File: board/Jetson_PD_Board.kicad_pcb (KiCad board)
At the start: 2 copper layers, 41.5 x 34.5 mm, 47 parts, among them J1 USB4081-03-A, J2 768250002, Q1 NTTFS5C673NLTAG, Q2 NTTFS5C673NLTAG, Q3 NTTFS5C673NLTAG, U1 APK43070DKZ-13-FA01, U2 USBLC6-2SC6

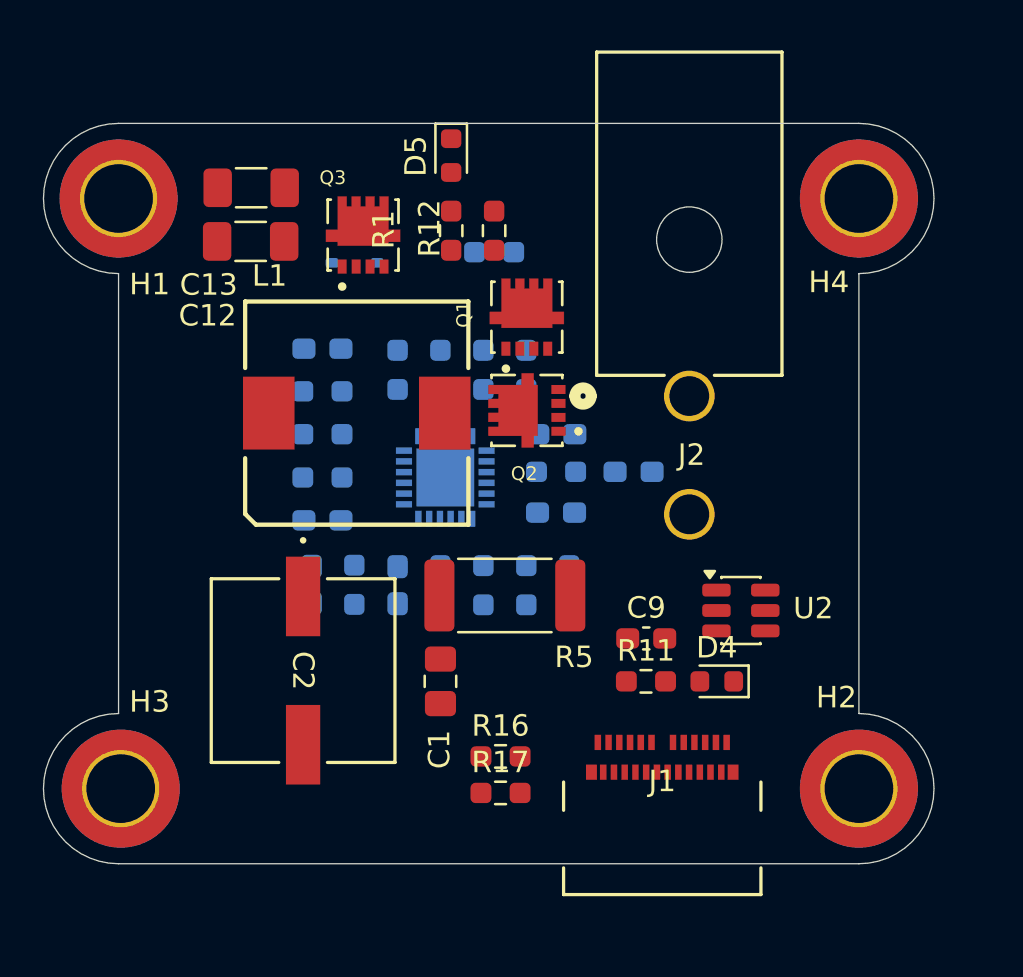
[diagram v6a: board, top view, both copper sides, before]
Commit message: Arranged power components
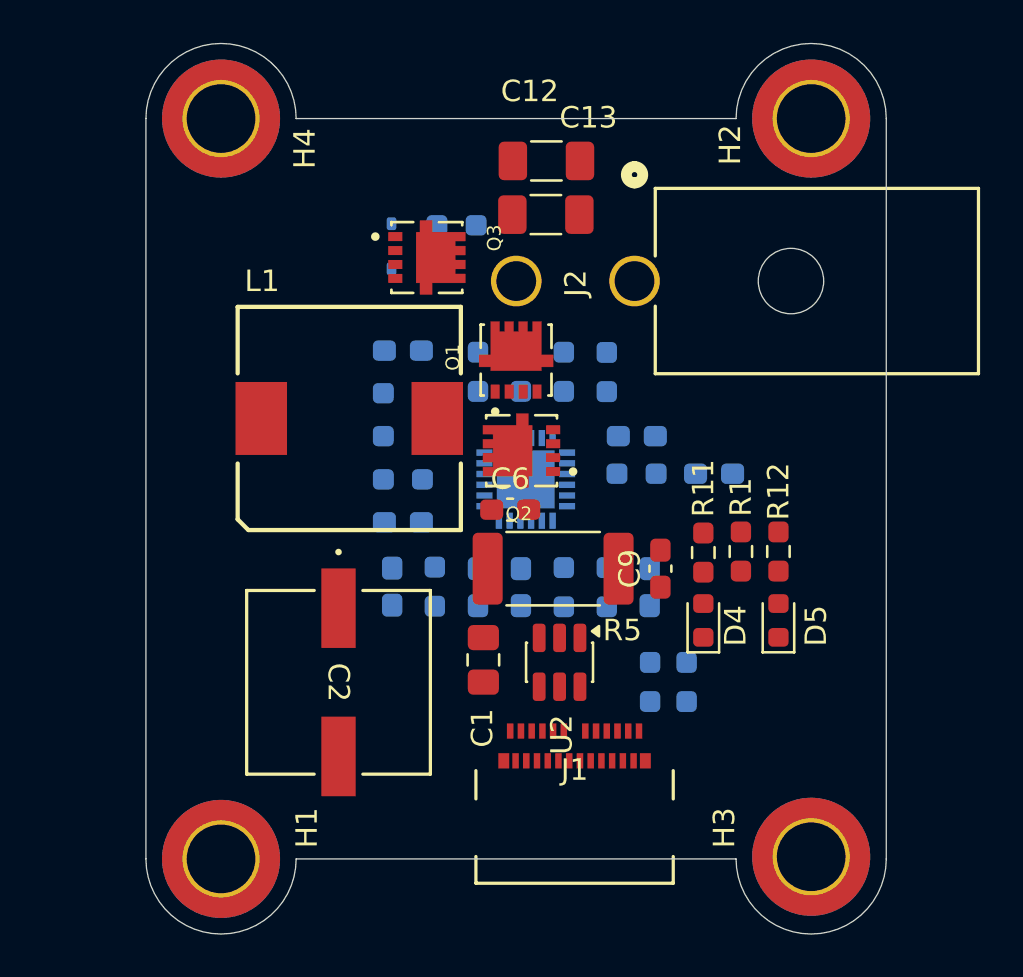
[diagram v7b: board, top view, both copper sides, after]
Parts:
- C6: moved to F.Cu
- R16, R17: moved to B.Cu
- moved H3 32.3 mm to (137.3, 114.7), turned to 90 degrees
- moved H2 31.3 mm to (137.3, 80.3), turned to -90 degrees
- moved H1 31.1 mm to (109.8, 114.8), turned to -90 degrees
- moved H4 30.0 mm to (109.8, 80.3), turned to 90 degrees
- moved D5 26.5 mm to (135.8, 103.7), turned to 90 degrees
- moved R1 20.1 mm to (134.0, 100.5)
- moved R12 20.0 mm to (135.8, 100.5)
- moved C12 14.3 mm to (124.9, 82.2), turned to 0 degrees
- moved C13 13.8 mm to (124.9, 84.8), turned to 0 degrees
- moved R17 10.1 mm to (131.5, 106.5), turned to -90 degrees
- moved U2 8.79 mm to (125.5, 105.6), turned to -90 degrees
- moved R16 7.79 mm to (129.8, 106.5), turned to -90 degrees
- moved R11 6.57 mm to (132.2, 100.5), turned to -90 degrees
- moved J2 5.94 mm to (129.0, 87.8), turned to 90 degrees
- moved J1 4.12 mm to (126.2, 112.2)
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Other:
- board size 41.5 x 34.5 mm -> 34.5 x 41.5 mm

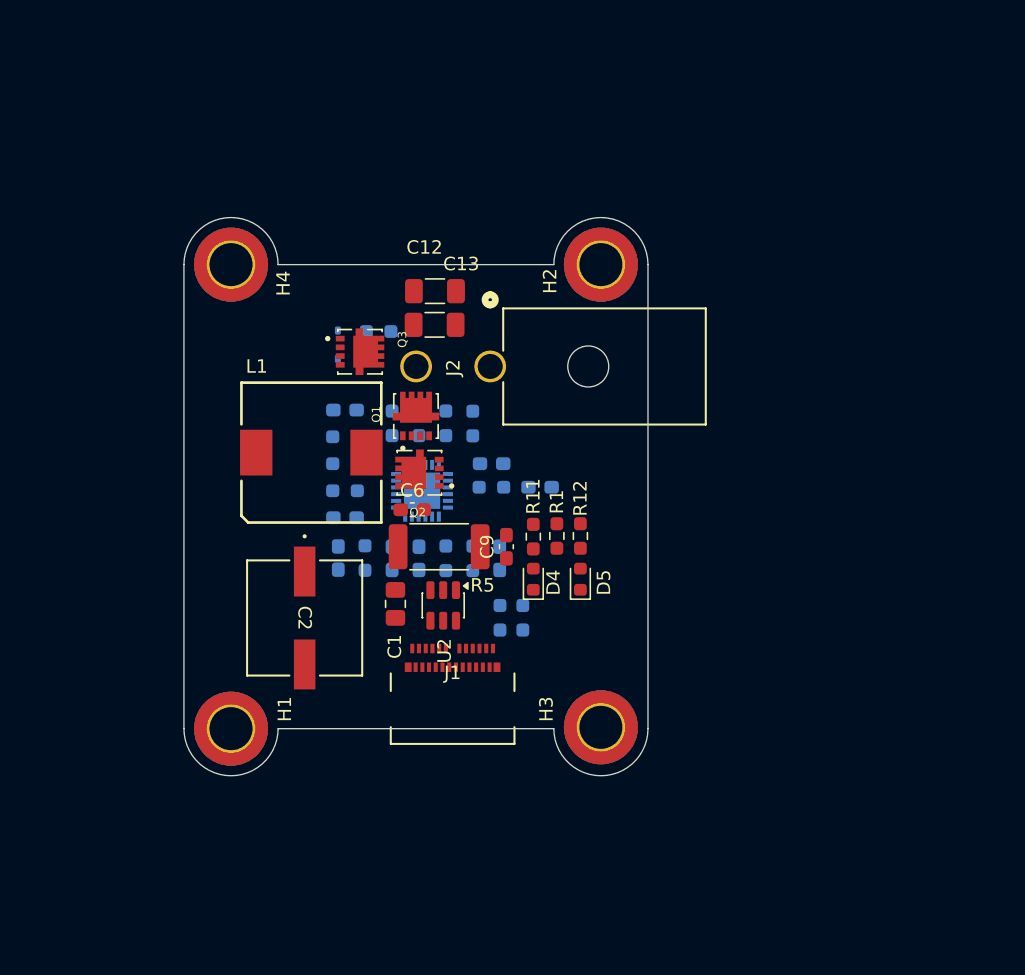
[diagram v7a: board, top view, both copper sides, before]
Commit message: Rearranged layout to be longer
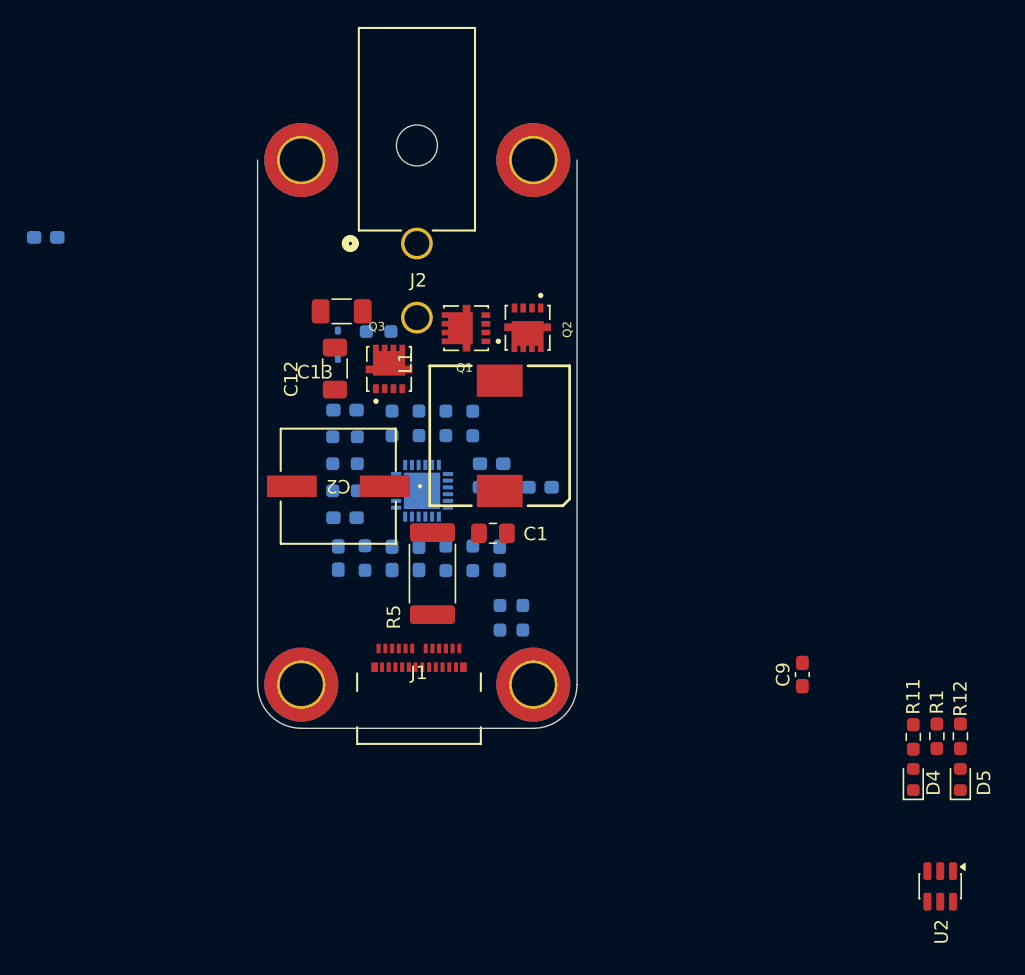
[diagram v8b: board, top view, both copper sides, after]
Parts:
- C6: moved to B.Cu
- moved U2 42.4 mm to (162.5, 126.5)
- moved C6 34.0 mm to (96.0, 78.2), turned to 180 degrees
- moved D4 31.9 mm to (160.5, 118.5)
- moved D5 31.9 mm to (164.0, 118.5)
- moved R1 31.9 mm to (162.2, 115.3)
- moved R11 31.9 mm to (160.5, 115.4)
- moved R12 31.9 mm to (164.0, 115.3)
- moved C9 24.0 mm to (152.2, 110.8)
- moved L1 14.1 mm to (129.8, 93.0), turned to -90 degrees
- moved Q2 13.5 mm to (131.8, 85.0), turned to -90 degrees
- moved J2 10.6 mm to (123.6, 78.7), turned to 180 degrees
- moved C2 10.1 mm to (117.8, 96.8), turned to 180 degrees
- moved C12 9.40 mm to (117.5, 88.0), turned to 90 degrees
- moved H4 9.37 mm to (115.0, 72.5)
- moved H2 9.26 mm to (132.2, 72.5)
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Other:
- board size 34.5 x 41.5 mm -> 23.8 x 42.2 mm
